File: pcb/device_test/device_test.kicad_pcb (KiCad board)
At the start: 4 copper layers, 80 x 80 mm, 21 parts, among them J101 Screw_Terminal_01x02, J201 USB_C_Receptacle_USB2.0_16P, J202 Conn_01x04, J203 Conn_02x10_Row_Letter_First, J301 USB_C_Receptacle_USB2.0_16P, J302 Conn_02x10_Row_Letter_First

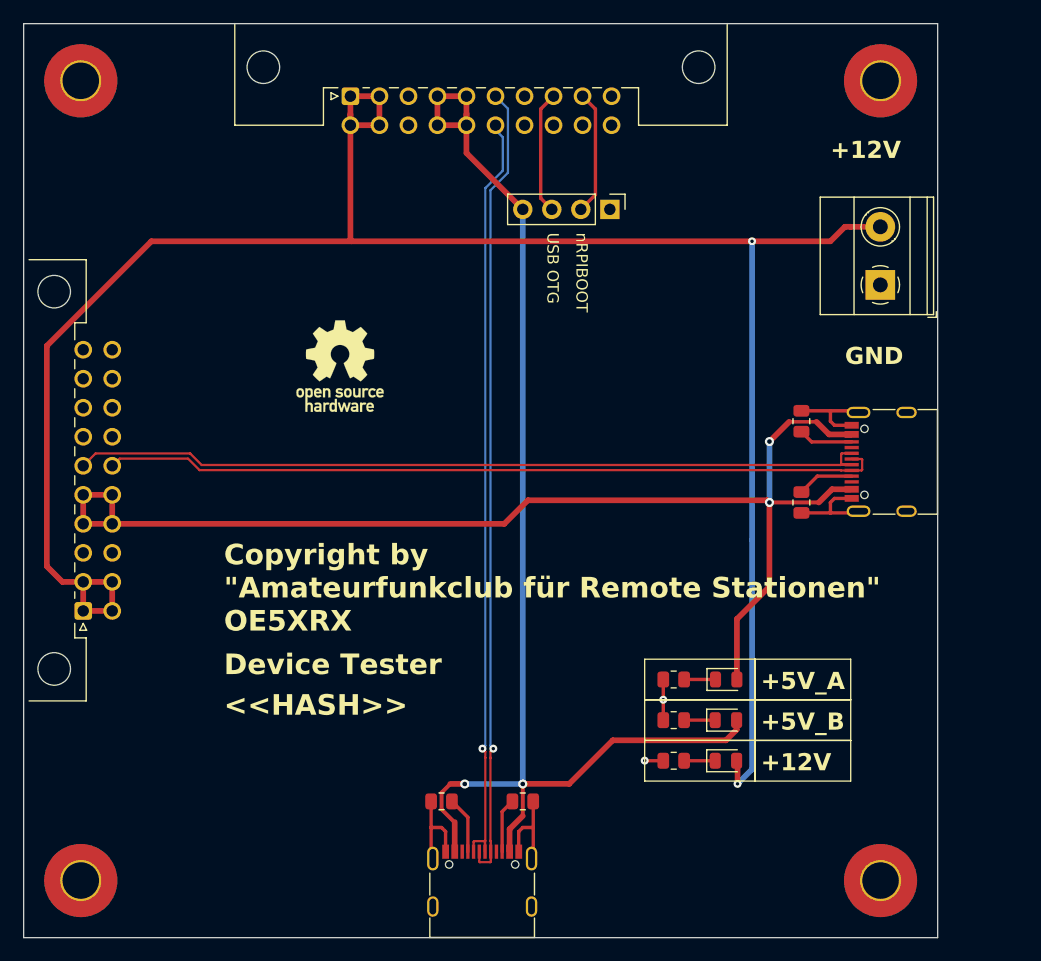
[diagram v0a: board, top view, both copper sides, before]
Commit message: update footprint lib name & change connector footprint
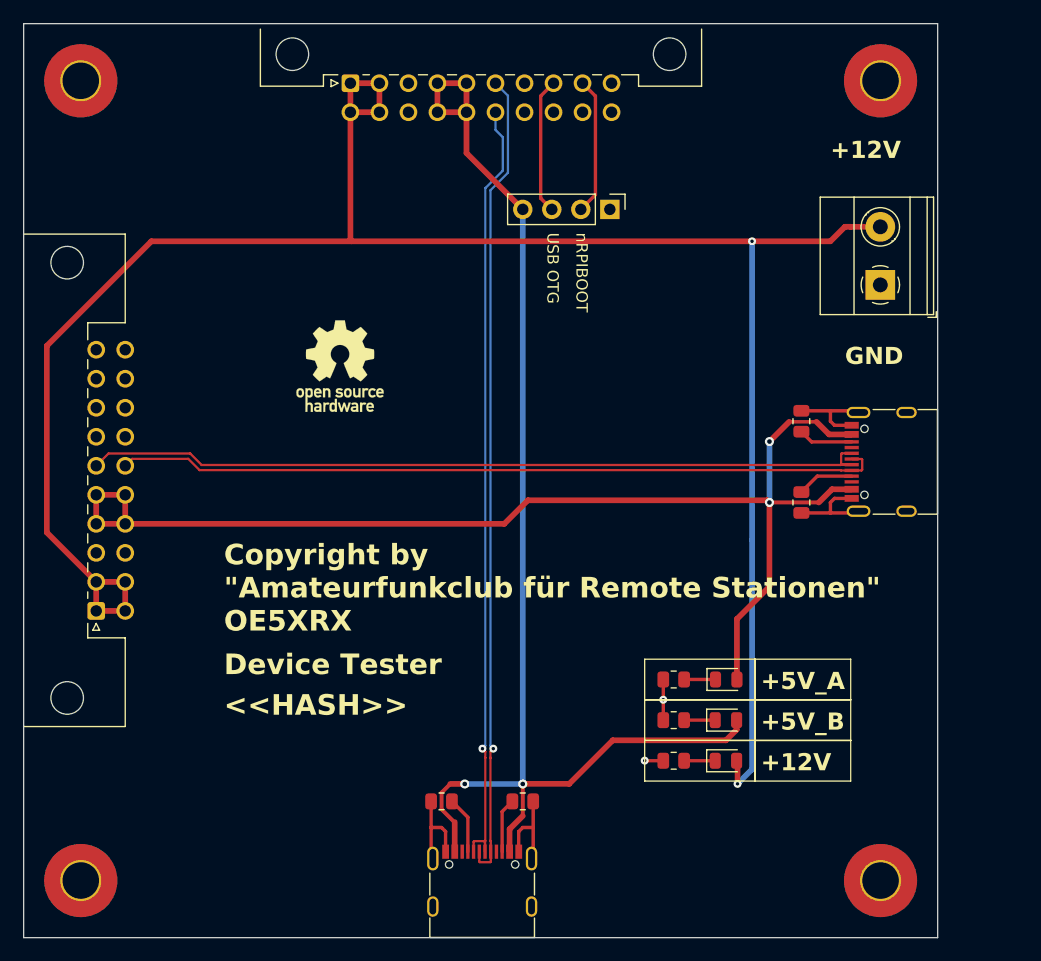
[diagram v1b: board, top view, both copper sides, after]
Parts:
- J203: footprint USB:PCN10C-20S-2.54DS -> PRJ:PCN10-20P-2.54DS
- J302: footprint USB:PCN10-20P-2.54DS -> PRJ:PCN10C-20S-2.54DS
- moved J203 1.14 mm to (144.4, 68.5)
- moved J302 1.14 mm to (122.1, 114.6)
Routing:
- net /Bus Tester Connector/USB-: track 68.2 -> 67.0 mm
- net /Device Tester Connector/USB_OTG_ID: track 10.8 -> 11.9 mm
- net /Device Tester Connector/USB-: track 67.5 -> 68.6 mm
- net /Device Tester Connector/USB+: track 70.2 -> 71.3 mm
- net /Bus Tester Connector/USB+: track 70.9 -> 69.8 mm
- net +5V_B: track 106.7 -> 105.5 mm
- net /Device Tester Connector/nRPIBOOT: track 10.9 -> 12.0 mm

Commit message: fix pin assignment
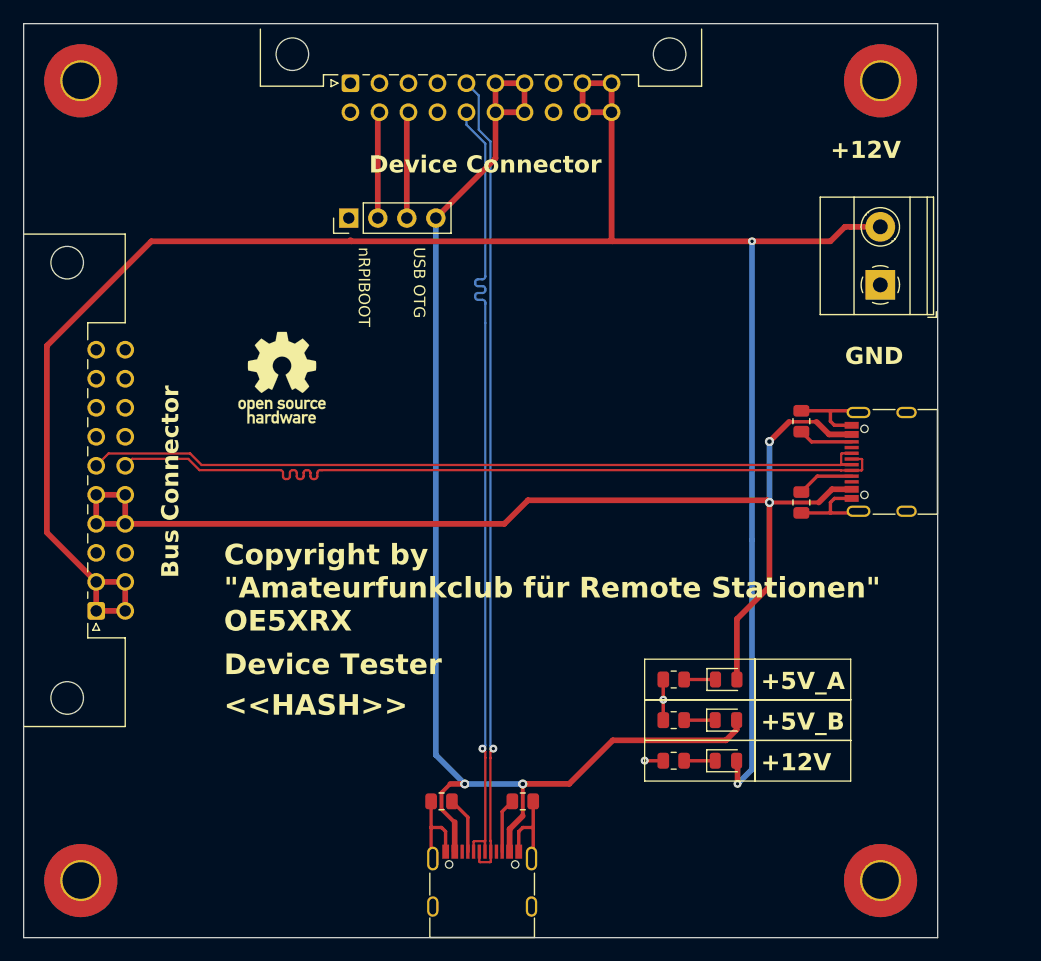
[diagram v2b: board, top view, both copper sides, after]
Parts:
- moved J202 22.9 mm to (144.2, 80.3), turned to 90 degrees
- moved #SYM101 5.18 mm to (138.4, 94.2)
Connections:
- J203 pad a1: +12V -> GND
- J203 pad a10: GND -> +12V
- J203 pad a2: +12V -> unconnected-(J203-Pin_a2-Pada2)
- J203 pad a3: GND -> unconnected-(J203-Pin_a3-Pada3)
- J203 pad a4: +5V_A -> unconnected-(J203-Pin_a4-Pada4)
- J203 pad a5: +5V_A -> /Device Tester Connector/USB+
- J203 pad a6: /Device Tester Connector/USB+ -> +5V_A
- J203 pad a7: unconnected-(J203-Pin_a7-Pada7) -> +5V_A
- J203 pad a8: /Device Tester Connector/USB_OTG_ID -> GND
- J203 pad a9: /Device Tester Connector/nRPIBOOT -> +12V
- J203 pad b1: +12V -> GND
- J203 pad b10: GND -> +12V
- J203 pad b2: +12V -> /Device Tester Connector/nRPIBOOT
- J203 pad b3: GND -> /Device Tester Connector/USB_OTG_ID
- J203 pad b4: +5V_A -> unconnected-(J203-Pin_b4-Padb4)
- J203 pad b5: +5V_A -> /Device Tester Connector/USB-
- J203 pad b6: /Device Tester Connector/USB- -> +5V_A
- J203 pad b7: unconnected-(J203-Pin_b7-Padb7) -> +5V_A
- J203 pad b8: unconnected-(J203-Pin_b8-Padb8) -> GND
- J203 pad b9: unconnected-(J203-Pin_b9-Padb9) -> +12V
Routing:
- net /Bus Tester Connector/USB-: track 67.0 -> 70.4 mm
- net /Device Tester Connector/nRPIBOOT: track 12.0 -> 9.32 mm
- net /Device Tester Connector/USB_OTG_ID: track 11.9 -> 9.32 mm
- net /Device Tester Connector/USB-: track 68.6 -> 71.1 mm
- net +5V_A: track 112.0 -> 113.2 mm
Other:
- board text added: "Bus Connector"
- board text added: "Device Connector"

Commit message: update
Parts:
- moved D301 3.56 mm to (177.2, 124.2)
- moved R303 3.56 mm to (172.6, 124.2)
- moved D201 3.56 mm to (177.2, 120.7)
- moved R203 3.56 mm to (172.7, 120.7)
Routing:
- net +5V_A: track 113.2 -> 117.5 mm
- net +5V_B: track 105.5 -> 109.1 mm
- net /Bus Tester Connector/USB-: track 70.4 -> 69.7 mm
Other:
- board text added: "+5V A"
- board text added: "+5V B"
- board text added: "A"
- board text added: "B"
- board text removed: "+5V_A"
- board text removed: "+5V_B"
